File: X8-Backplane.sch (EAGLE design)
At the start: 0 parts

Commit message: Added part for raspberry pi, 5V -> 3.3V buck converter, and IMU pins
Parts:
- added C10, C6, C9: 150uF, PowerComponents:C-TANTALUM(10UF_150UF)
- added C11, C12, C13, C2: 10uF, PowerComponents:C-TANTALUM(10UF_150UF)
- added C3: 0.47uF, SparkFun-Capacitors:CAP0805
- added C4: 0.01uF, SparkFun-Passives:CAP0603-CAP
- added PCB1: RPI2, MicrocontrollerComponents:RPI2
- added U$1: SWITCHMODE_SCHOTTKY, PowerComponents:SWITCHMODE_SCHOTTKY
- added U$2: 15uH, DiscreteComponents:HCMA1305
- added U$3: BNO055_9DOF_BREAKOUT, Other:BNO055_9DOF_BREAKOUT
- added U1: LM2678, PowerComponents:LM2678
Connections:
- new net +12V: C11.+, C12.+, C13.+, C2.+, C3.1, U1.VIN
- new net +5V: C10.+, C6.+, C9.+, U$2.2, U1.FEEDBACK
- new net GND: C10.-, C11.-, C12.-, C13.-, C2.-, C3.2, C6.-, C9.-, U$1.P$1, U$1.P$3, U1.GND, U1.TABGND
- new net N$2: C4.1, U1.BOOST
- new net N$3: C4.2, U$1.P$4, U$2.1, U1.OUTPUT
- new net N$4: PCB1.3V3@1

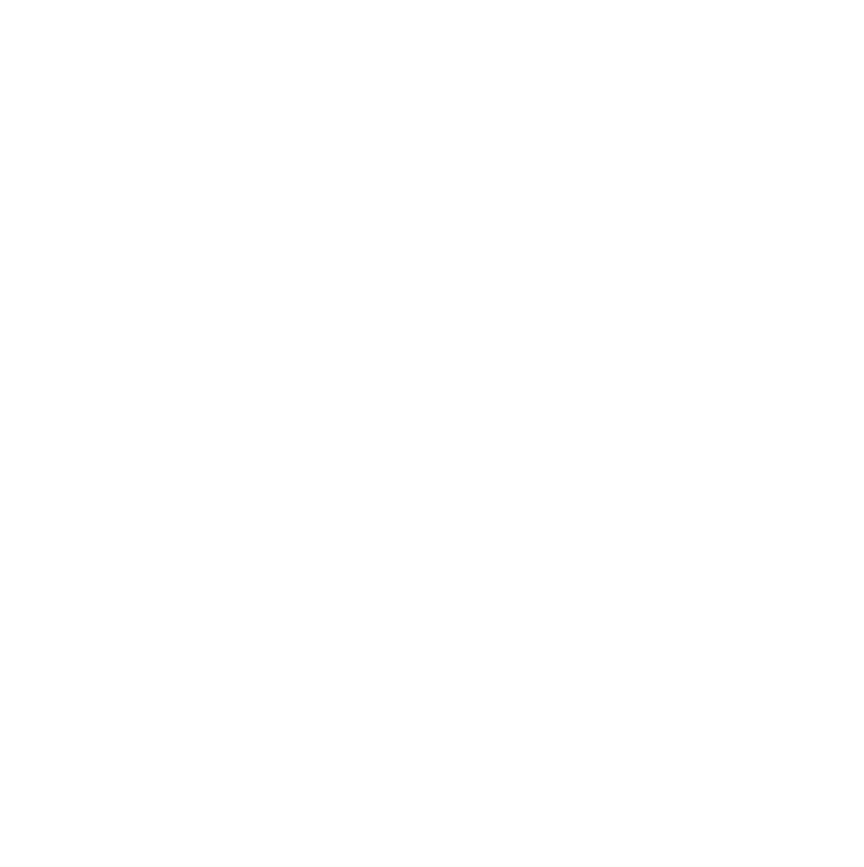
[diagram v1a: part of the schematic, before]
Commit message: added brd to brd connector
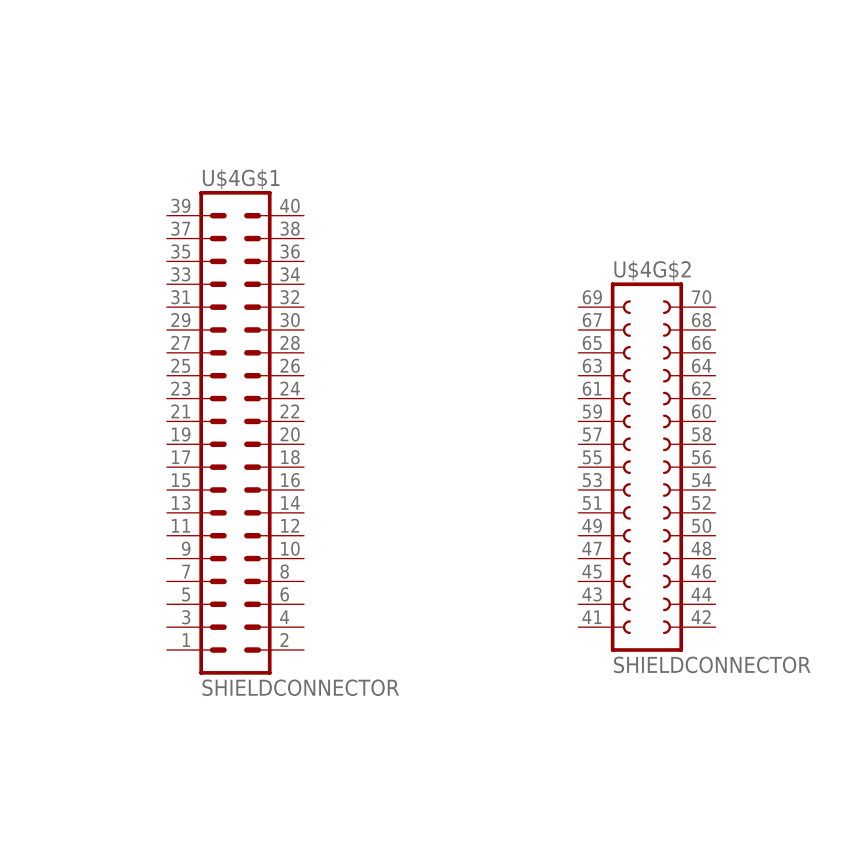
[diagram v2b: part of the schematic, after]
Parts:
- added U$4: SHIELDCONNECTOR, backplane_to_shield_connector:SHIELDCONNECTOR
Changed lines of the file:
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@@
 <part name="P+4" library="supply1" deviceset="+5V" device=""/>
 <part name="U$3" library="Other" deviceset="BNO055_9DOF_BREAKOUT" device=""/>
+<part name="U$4" library="backplane_to_shield_connector" deviceset="SHIELDCONNECTOR" device=""/>
 </parts>
 <sheets>
@@
 </instance>
 <instance part="U$3" gate="G$1" x="347.98" y="165.1"/>
+<instance part="U$4" gate="G$1" x="373.38" y="91.44"/>
+<instance part="U$4" gate="G$2" x="419.1" y="88.9"/>
 </instances>
 <busses>

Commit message: because I can
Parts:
- added IC1: MAX3467CPA, maxim:MAX3467CPA
- added U$7: PCA9615, test_lib:PCA9615
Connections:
- new net +3V3: IC1.VCC
- new net COM_A: IC1.A
- new net COM_B: IC1.B
- new net COM_Y: IC1.Y
- new net COM_Z: IC1.Z
- new net TETHER_RX: IC1.RO
- new net TETHER_TX: IC1.DI
- net GND: now also IC1.GND
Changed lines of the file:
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@@
 <part name="U$3" library="Other" deviceset="BNO055_9DOF_BREAKOUT" device=""/>
 <part name="U$4" library="backplane_to_shield_connector" deviceset="SHIELDCONNECTOR" device=""/>
+<part name="IC1" library="maxim" deviceset="MAX3467*" device="PA" technology="C"/>
+<part name="+3V1" library="supply1" deviceset="+3V3" device=""/>
+<part name="GND1" library="supply1" deviceset="GND" device=""/>
+<part name="U$7" library="test_lib" deviceset="PCA9615" device=""/>
 </parts>
 <sheets>
@@
 <instance part="U$4" gate="G$1" x="373.38" y="91.44"/>
 <instance part="U$4" gate="G$2" x="419.1" y="88.9"/>
+<instance part="IC1" gate="G$1" x="496.57" y="172.72"/>
+<instance part="+3V1" gate="G$1" x="513.08" y="191.77"/>
+<instance part="GND1" gate="1" x="513.08" y="153.67"/>
+<instance part="U$7" gate="G$1" x="408.94" y="165.1"/>
 </instances>
 <busses>
@@
 <junction x="68.58" y="-137.16"/>
 </segment>
+<segment>
+<pinref part="IC1" gate="G$1" pin="GND"/>
+<wire x1="509.27" y1="160.02" x2="513.08" y2="160.02" width="0.1524" layer="91"/>
+<wire x1="513.08" y1="160.02" x2="513.08" y2="156.21" width="0.1524" layer="91"/>
+<pinref part="GND1" gate="1" pin="GND"/>
+</segment>
 </net>
 <net name="+12V" class="0">
@@
 </segment>
 </net>
+<net name="+3V3" class="0">
+<segment>
+<pinref part="IC1" gate="G$1" pin="VCC"/>
+<wire x1="509.27" y1="185.42" x2="513.08" y2="185.42" width="0.1524" layer="91"/>
+<wire x1="513.08" y1="185.42" x2="513.08" y2="189.23" width="0.1524" layer="91"/>
+<pinref part="+3V1" gate="G$1" pin="+3V3"/>
+</segment>
+</net>
+<net name="TETHER_RX" class="0">
+<segment>
+<pinref part="IC1" gate="G$1" pin="RO"/>
+<wire x1="486.41" y1="167.64" x2="485.14" y2="167.64" width="0.1524" layer="91"/>
+<label x="485.14" y="167.64" size="1.27" layer="95" rot="R180" xref="yes"/>
+</segment>
+</net>
+<net name="TETHER_TX" class="0">
+<segment>
+<label x="485.14" y="177.8" size="1.27" layer="95" rot="R180" xref="yes"/>
+<pinref part="IC1" gate="G$1" pin="DI"/>
+<wire x1="485.14" y1="177.8" x2="486.41" y2="177.8" width="0.1524" layer="91"/>
+</segment>
+</net>
+<net name="COM_A" class="0">
+<segment>
+<pinref part="IC1" gate="G$1" pin="A"/>
+<wire x1="509.27" y1="170.18" x2="513.08" y2="170.18" width="0.1524" layer="91"/>
+<label x="513.08" y="170.18" size="1.27" layer="95" xref="yes"/>
+</segment>
+</net>
+<net name="COM_B" class="0">
+<segment>
+<pinref part="IC1" gate="G$1" pin="B"/>
+<wire x1="509.27" y1="165.1" x2="513.08" y2="165.1" width="0.1524" layer="91"/>
+<label x="513.08" y="165.1" size="1.27" layer="95" xref="yes"/>
+</segment>
+</net>
+<net name="COM_Y" class="0">
+<segment>
+<pinref part="IC1" gate="G$1" pin="Y"/>
+<wire x1="509.27" y1="180.34" x2="513.08" y2="180.34" width="0.1524" layer="91"/>
+<label x="513.08" y="180.34" size="1.27" layer="95" xref="yes"/>
+</segment>
+</net>
+<net name="COM_Z" class="0">
+<segment>
+<pinref part="IC1" gate="G$1" pin="Z"/>
+<wire x1="509.27" y1="175.26" x2="513.08" y2="175.26" width="0.1524" layer="91"/>
+<label x="513.08" y="175.26" size="1.27" layer="95" xref="yes"/>
+</segment>
+</net>
